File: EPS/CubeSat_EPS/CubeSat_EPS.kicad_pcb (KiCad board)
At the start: 2 copper layers, 84 x 84 mm, 32 parts, among them J1 SOLAR_IN, J10 AUX_POWER_OUT, J11 INA226_MODULE, J12 ADCS_5V_POWER, J2 CN3722_2S_MPPT_MODULE, J3 BMS_MODULE, J4 BATTERY_PACK, J5 BUCK_5V_MODULE, J6 OBC_INTERFACE, J7 BUCK_3V3_MODULE, J8 ADCS_POWER, J9 TTC_POWER, Q1 P-MOSFET

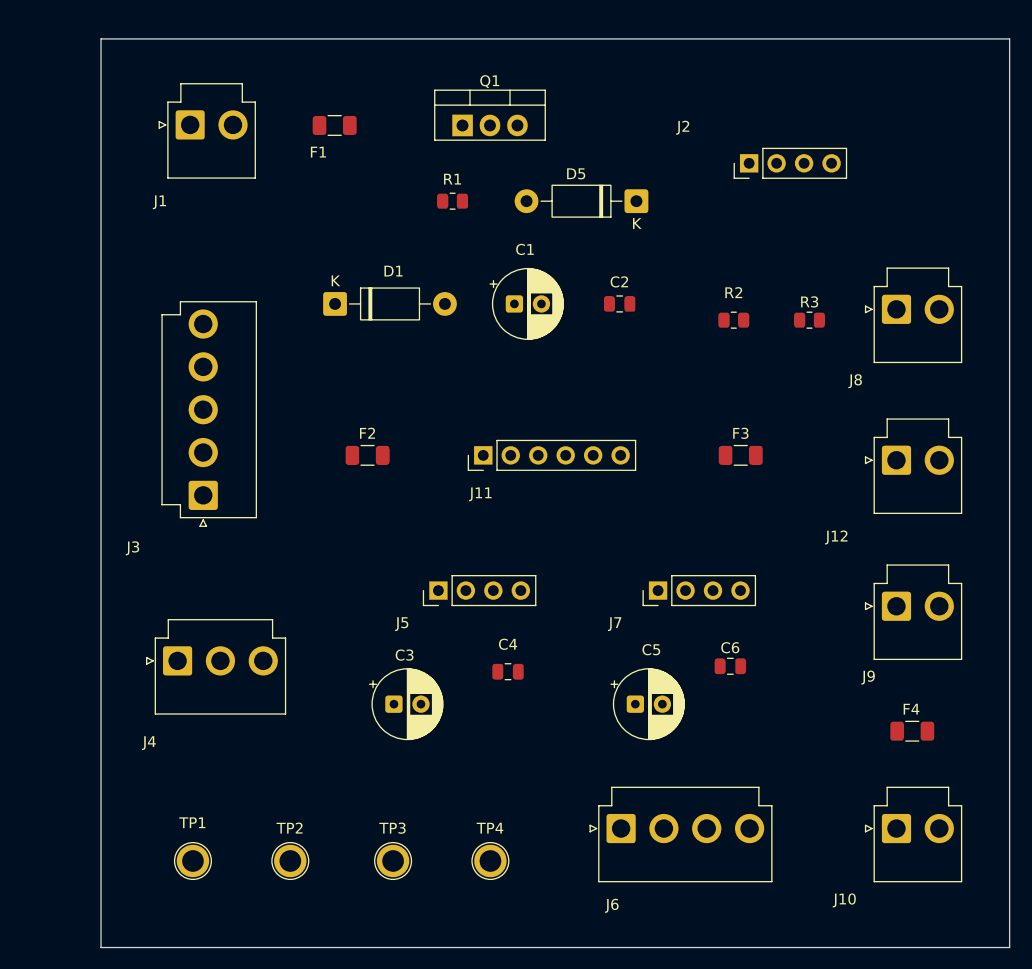
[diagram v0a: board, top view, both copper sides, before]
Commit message: Fix: Move EPS files to correct folder (EPS/CubeSat_EPS/)
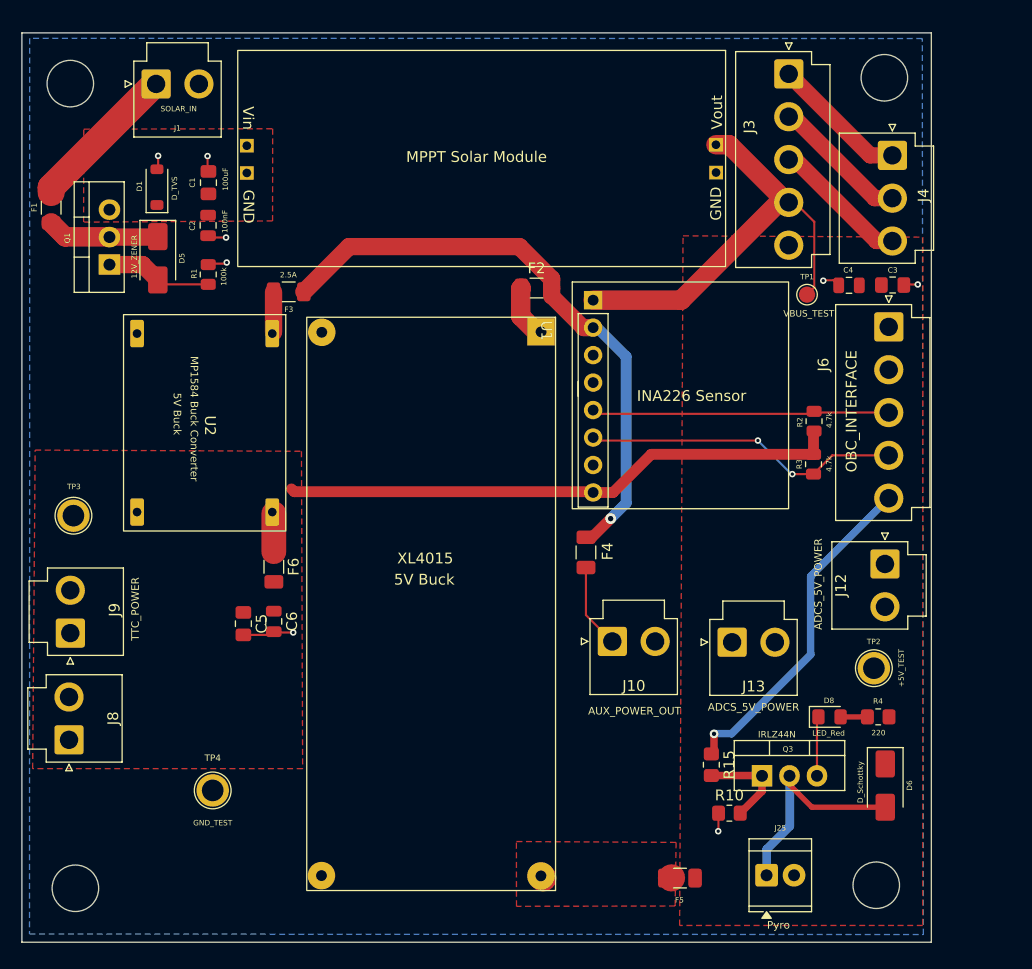
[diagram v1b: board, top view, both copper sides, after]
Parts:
- removed J11: INA226_MODULE, Connector_PinHeader_2.54mm:PinHeader_1x06_P2.54mm_Vertical
- removed J5: BUCK_5V_MODULE, Connector_PinHeader_2.54mm:PinHeader_1x04_P2.54mm_Vertical
- removed J7: BUCK_3V3_MODULE, Connector_PinHeader_2.54mm:PinHeader_1x04_P2.54mm_Vertical
- added D6: D_Schottky, Diode_SMD:D_SMA, F.Cu at (182.5, 120.5)
- added D8: LED_Red, LED_SMD:LED_0805_2012Metric_Pad1.15x1.40mm_HandSolder, F.Cu at (177.3, 114.2)
- added F5: 5A, Fuse:Fuse_1206_3216Metric, F.Cu at (163.5, 129.1)
- added F6: 3A, Fuse:Fuse_1206_3216Metric, F.Cu at (126.0, 100.3)
- added H1: MountingHole, MountingHole:MountingHole_4.3mm_M4, F.Cu at (107.2, 55.6)
- added H2: MountingHole, MountingHole:MountingHole_4.3mm_M4, F.Cu at (182.4, 55.1)
- added H3: MountingHole, MountingHole:MountingHole_4.3mm_M4, F.Cu at (181.7, 129.7)
- added H4: MountingHole, MountingHole:MountingHole_4.3mm_M4, F.Cu at (107.6, 130.0)
- added J13: ADCS_5V_POWER, Connector_JST:JST_VH_B2P-VH-B_1x02_P3.96mm_Vertical, F.Cu at (168.3, 107.3)
- added J25: Pyro, TerminalBlock_TE-Connectivity:TerminalBlock_TE_282834-2_1x02_P2.54mm_Horizontal, F.Cu at (171.5, 128.8)
- added Q3: IRLZ44N, Package_TO_SOT_THT:TO-220-3_Vertical, F.Cu at (171.1, 119.6)
- added R10: 10k, Resistor_SMD:R_0805_2012Metric_Pad1.20x1.40mm_HandSolder, F.Cu at (168.1, 123.1)
- added R15: 100 ohm, Resistor_SMD:R_0805_2012Metric_Pad1.20x1.40mm_HandSolder, F.Cu at (166.4, 118.6)
- added R4: 220, Resistor_SMD:R_0805_2012Metric_Pad1.20x1.40mm_HandSolder, F.Cu at (181.8, 114.2)
- added U1: XL4015, 815-2:XL4015 Buck, F.Cu at (152.0, 77.2)
- added U2: MP1584 Buck Converter, MP1584:MP1584 module 20mm_15mm, F.Cu at (119.6, 87.2)
- added U3: CN3722_2S_MPPT_MODULE, 815-2:MPPT Solar, F.Cu at (122.7, 52.6)
- C1, C3, C5: footprint Capacitor_THT:CP_Radial_D6.3mm_P2.50mm -> Capacitor_SMD:C_0805_2012Metric_Pad1.18x1.45mm_HandSolder
- D1: footprint Diode_THT:D_DO-41_SOD81_P10.16mm_Horizontal -> Diode_SMD:D_SOD-123
- D5: footprint Diode_THT:D_DO-41_SOD81_P10.16mm_Horizontal -> Diode_SMD:D_SMA
- F2: value TBD -> 5A
- F3: value TBD -> 2.5A
- J2: value CN3722_2S_MPPT_MODULE -> INA226_MODULE; footprint Connector_PinHeader_2.54mm:PinHeader_1x04_P2.54mm_Vertical -> 815-2:INA226 Current Sensor
- J6: footprint Connector_JST:JST_VH_B4P-VH_1x04_P3.96mm_Vertical -> Connector_JST:JST_VH_B5P-VH_1x05_P3.96mm_Vertical
- TP1: footprint TestPoint:TestPoint_Plated_Hole_D2.0mm -> TestPoint:TestPoint_Pad_D1.5mm
- moved J8 86.2 mm to (107.0, 116.3), turned to 90 degrees
- moved J4 80.9 mm to (183.2, 62.3), turned to -90 degrees
- moved TP1 77.2 mm to (175.3, 75.1)
- moved J9 76.4 mm to (107.2, 106.4), turned to 90 degrees
- moved J3 66.7 mm to (173.6, 54.7), turned to -90 degrees
- moved C3 60.2 mm to (183.2, 74.2)
- moved TP2 56.8 mm to (181.4, 109.7)
- moved J6 52.6 mm to (182.8, 78.1), turned to -90 degrees
- moved C4 47.6 mm to (179.2, 74.3), turned to 180 degrees
- moved D5 44.6 mm to (115.2, 71.8), turned to -90 degrees
- moved F3 44.4 mm to (127.3, 74.9), turned to 180 degrees
- moved TP3 43.5 mm to (107.5, 95.6)
- moved C6 42.4 mm to (126.0, 105.3), turned to -90 degrees
- moved C2 38.7 mm to (119.9, 68.7), turned to -90 degrees
- moved C5 37.0 mm to (123.2, 105.6), turned to -90 degrees
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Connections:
- J2 pad 1: /MPPT_IN+ -> /VBUS
- J2 pad 2: GND -> /VBUS_DIST
- J2 pad 3: /VBUS -> unconnected-(J2-Pin_3-Pad3)
- J2 pad 4: GND -> unconnected-(J2-Pin_4-Pad4)
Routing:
- net /VBUS_DIST: track 0.00 -> 55.2 mm, vias 0 -> 1
- net /+3V3: track 0.00 -> 52.0 mm
- net /VBUS: track 0.00 -> 41.0 mm
- net /Ras-pie_input: track 0.00 -> 31.4 mm, vias 0 -> 1
- net /SCL: track 0.00 -> 29.5 mm, vias 0 -> 2
- net /SDA: track 0.00 -> 27.6 mm
- net GND: track 0.00 -> 21.2 mm, vias 0 -> 8
- net /DRAIN: track 0.00 -> 20.6 mm
- net Net-(J1-Pin_1): track 0.00 -> 14.1 mm
- net /BATT-: track 0.00 -> 12.7 mm
- net /BATT+: track 0.00 -> 12.7 mm
- net /BATT_MID: track 0.00 -> 12.7 mm
- net Net-(D5-K): track 0.00 -> 10.8 mm
- net Net-(D5-A): track 0.00 -> 9.89 mm
- net /GATE: track 0.00 -> 9.02 mm
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- added copper zone on F.Cu, net /+3V3
- added copper zone on F.Cu, net /+5V
- added copper zone on F.Cu, net /MPPT_IN+
- added copper zone on B.Cu, net GND
- added copper zone on F.Cu, net Net-(U1-Vout)
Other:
- board size 84 x 84 mm -> 84.1 x 84.1 mm
- board text added: "5V Buck"

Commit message: fix: EPS dimensions written properly
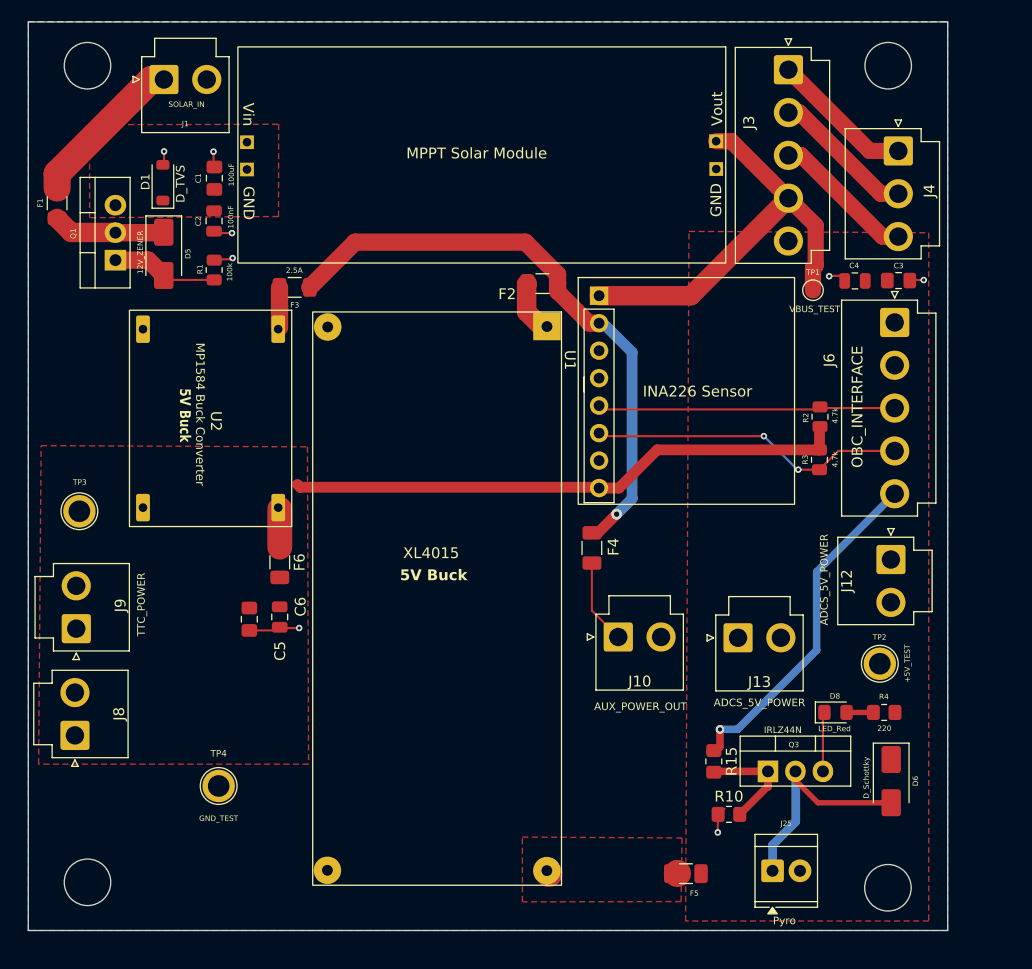
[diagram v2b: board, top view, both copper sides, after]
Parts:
- moved H1 2.30 mm to (108.8, 54.0)
- moved H4 1.25 mm to (108.8, 129.5)
- moved H2 1.17 mm to (182.8, 54.0)
- moved H3 1.11 mm to (182.8, 130.0)
- moved J1 0.84 mm to (115.8, 55.2)
- moved U1 0.74 mm to (152.6, 76.7)
- moved D6 0.69 mm to (183.1, 120.1)
- moved J12 0.69 mm to (183.0, 99.6)
- moved J13 0.69 mm to (168.9, 106.9)
- moved J6 0.69 mm to (183.4, 77.7)
- moved R2 0.69 mm to (176.5, 86.4)
- moved J4 0.69 mm to (183.7, 61.9)
- moved D8 0.69 mm to (177.9, 113.8)
- moved F2 0.69 mm to (150.8, 74.1)
- moved F3 0.69 mm to (127.9, 74.5)
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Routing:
- net /GATE: track 9.02 -> 10.2 mm
- net Net-(J1-Pin_1): track 14.1 -> 14.8 mm
- net /BATT+: track 12.7 -> 13.3 mm
- net /VBUS: track 41.0 -> 40.5 mm
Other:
- board size 84.1 x 84.1 mm -> 85 x 84 mm
